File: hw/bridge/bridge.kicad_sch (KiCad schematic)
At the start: 43 parts, among them J1 USB_C_Receptacle_USB2.0_14P, J2 DE9, U1 CH340E, U2 MAX485E, U3 CH334R, U4 74LVC2G04, U5 MCP1754S-3302xCB, U6 TJA1051T-3, Y1 HCI XC53G2-12.000-F20LJDT

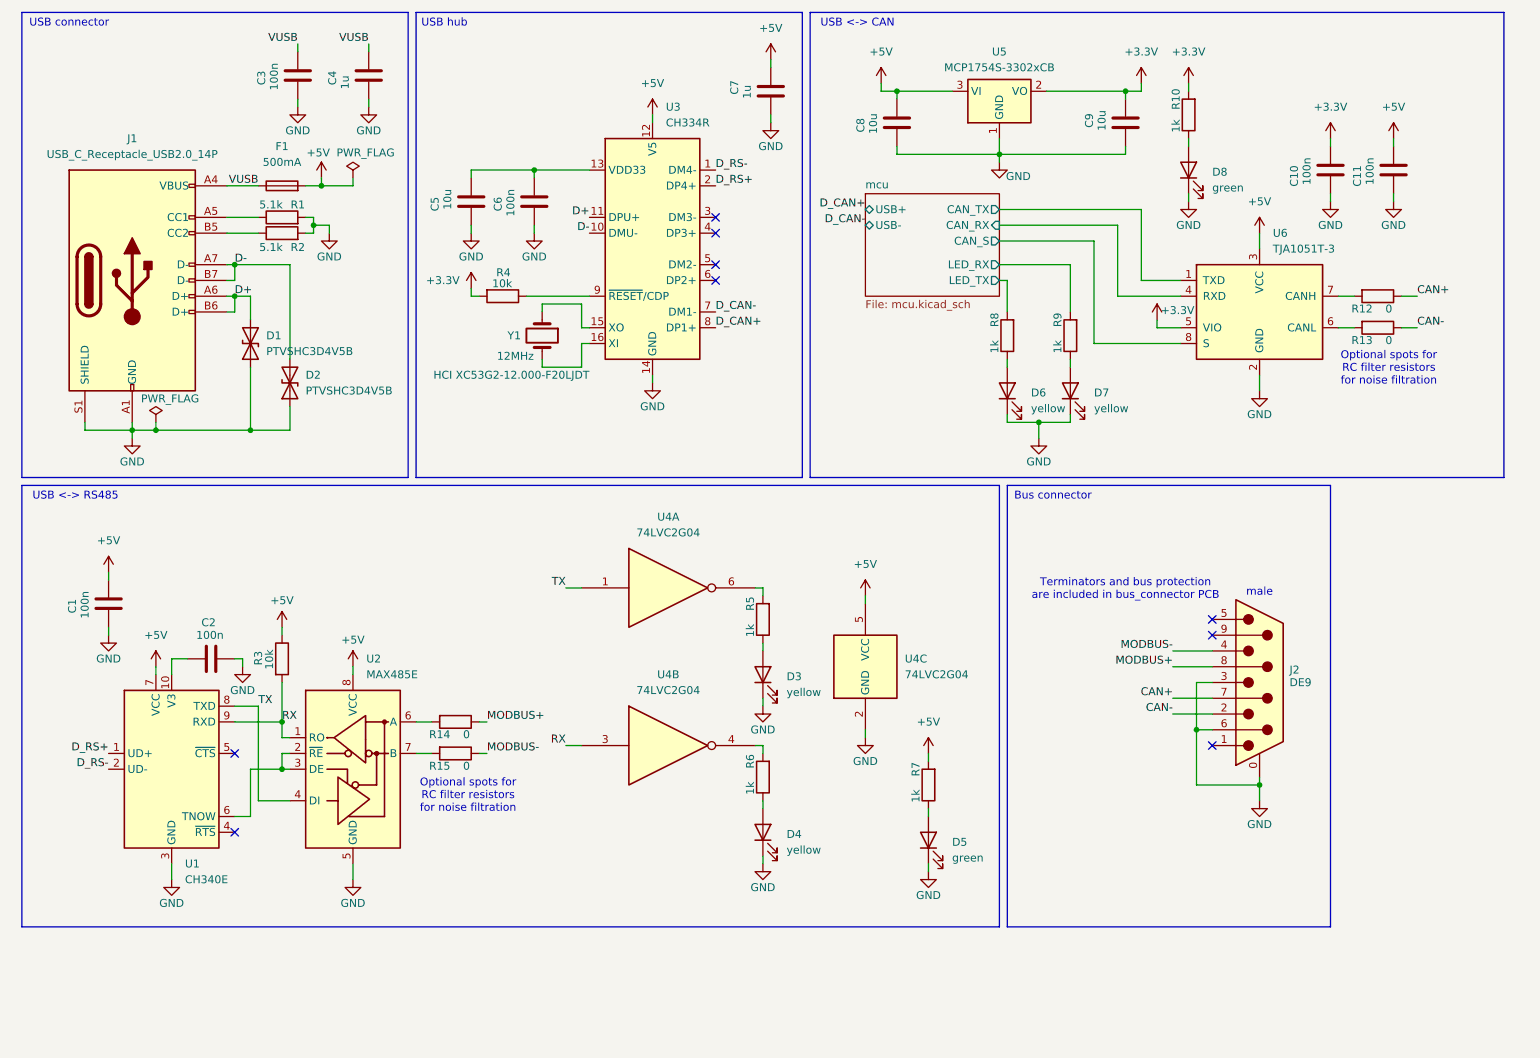
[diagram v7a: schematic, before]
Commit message: Add hub crystal-free alternative, add hub rst pull up, replace usbc with tht alternative
Signed-off-by: Mateusz Pająk <22417805+Tai-Min@users.noreply.github.com>
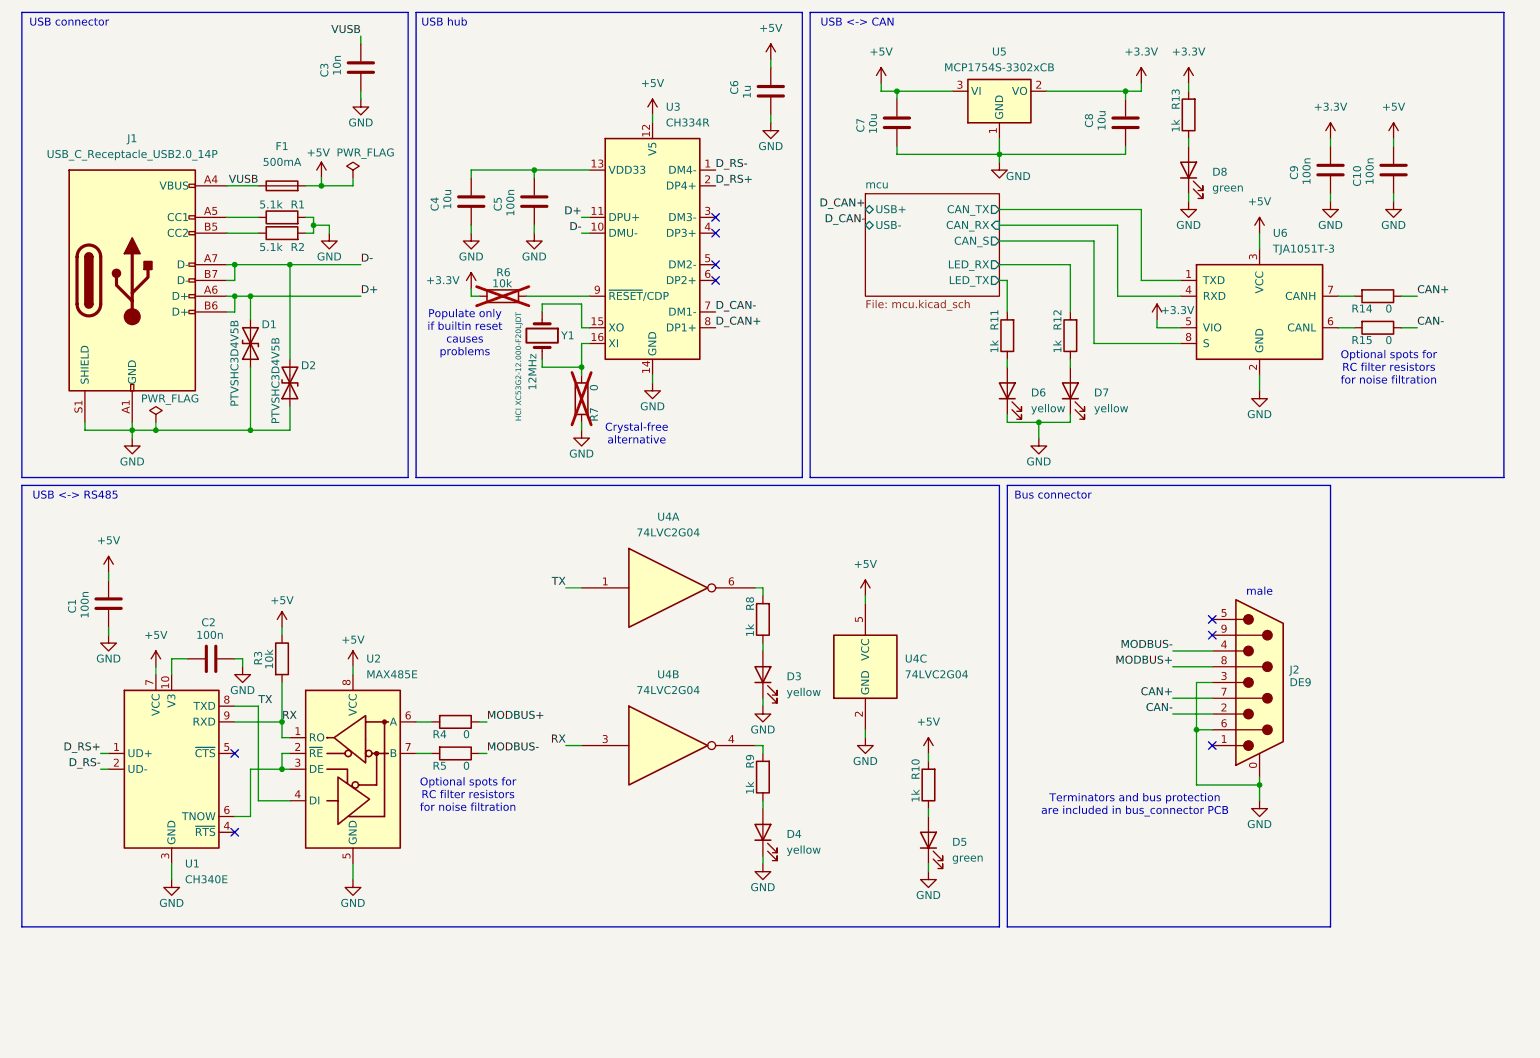
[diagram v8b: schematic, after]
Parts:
- removed C4: 1u, Capacitor_SMD:C_0603_1608Metric, symbol Device:C
- added R7: 0, Resistor_SMD:R_0603_1608Metric, symbol Device:R
- C3: value 100n -> 10n; LCSC https://www.lcsc.com/product-detail/C66501.html -> https://www.lcsc.com/product-detail/C100042.html
- J1: footprint Connector_USB:USB_C_Receptacle_Amphenol_12401610E4-2A_CircularHoles -> Connector_USB:USB_C_Receptacle_GCT_USB4085; LCSC https://www.lcsc.com/product-detail/C5119948.html?s_z=n_124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 -> https://www.lcsc.com/product-detail/C7095263.html?s_z=n_USB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
- R6: renamed from R4; now not fitted
- renumbered C11 to C10, C5 to C4, C6 to C5, C7 to C6, C8 to C7, C9 to C8, C10 to C9, R7 to R10, R8 to R11, R9 to R12, R10 to R13, R12 to R14, R13 to R15, R14 to R4, R15 to R5, R5 to R8, R6 to R9
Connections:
- net GND: now also R7.2
- net at U3.16 (XI), Y1.2: now also R7.1
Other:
- note added: "Crystal-free alternative"
- note added: "Populate only if builtin reset causes problems"
- moved on the sheet: C3
